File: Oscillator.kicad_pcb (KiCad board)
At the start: 2 copper layers, 19.3 x 14 mm, 11 parts, among them J1 Conn_01x01, J2 Conn_01x01, J3 Conn_01x01, J4 Conn_01x01, U1 74HC04, Y1 10 MHz

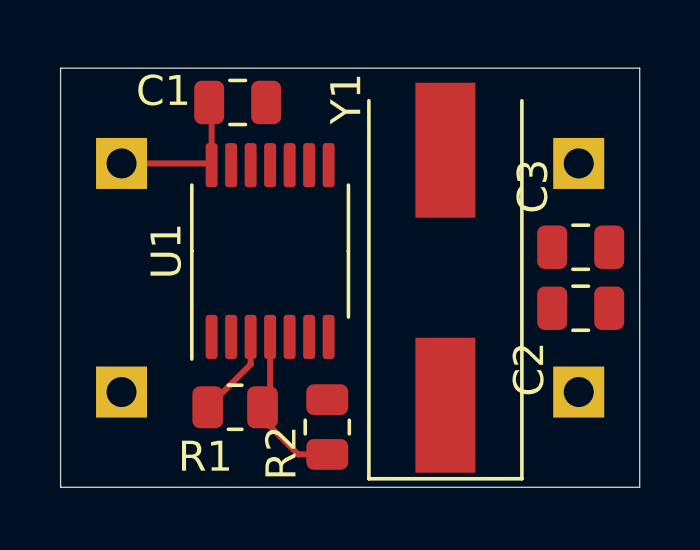
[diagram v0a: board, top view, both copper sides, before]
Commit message: routed all signals
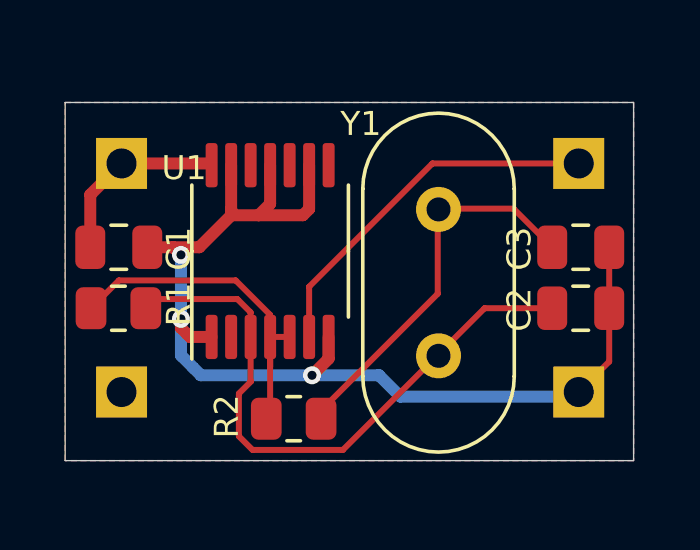
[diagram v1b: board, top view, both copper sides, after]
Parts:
- Y1: footprint Crystal:Crystal_SMD_HC49-SD -> Crystal:Crystal_HC49-U_Vertical
- moved C1 6.24 mm to (115.5, 95.5)
- moved R1 5.10 mm to (115.5, 97.5), turned to 180 degrees
- moved Y1 2.61 mm to (126.1, 99.1)
- moved R2 1.15 mm to (121.3, 101.2), turned to 0 degrees
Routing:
- net GND: track 0.00 -> 36.7 mm, vias 0 -> 3
- net Net-(C2-Pad1): track 2.94 -> 20.7 mm
- net Net-(C3-Pad1): track 0.00 -> 13.0 mm
- net /Out: track 0.00 -> 12.4 mm
- net Net-(R1-Pad2): track 5.48 -> 12.0 mm
- net VCC: track 5.15 -> 6.54 mm
- added copper zone on B.Cu, net GND
- added copper zone on F.Cu, net GND
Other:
- board size 19.3 x 14 mm -> 18.9 x 11.9 mm

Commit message: silkscreen improvements
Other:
- board text added: "github.com/daveho/ Oscillator"
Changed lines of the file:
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@@
     (property "ki_keywords" "HCMOS not inv")
     (attr smd)
-    (fp_text reference "U1" (at 2.7686 -2.8702 180) (layer "F.SilkS")
+    (fp_text reference "U1" (at 1.651 -3.429 180) (layer "F.SilkS")
         (effects (font (size 0.8 0.8) (thickness 0.15)))
     )
@@
     (property "ki_keywords" "quartz ceramic resonator oscillator")
     (attr through_hole)
-    (fp_text reference "Y1" (at 7.7332 -2.5908 180) (layer "F.SilkS")
+    (fp_text reference "Y1" (at 7.5808 -2.6924 180) (layer "F.SilkS")
         (effects (font (size 0.8 0.8) (thickness 0.15)))
     )
@@
     (property "ki_keywords" "connector")
     (attr through_hole)
-    (fp_text reference "J2" (at 2.667 0) (layer "B.SilkS")
-        (effects (font (size 1 1) (thickness 0.15)) (justify mirror))
+    (fp_text reference "J2" (at 2.032 -1.2192) (layer "F.SilkS")
+        (effects (font (size 0.8 0.8) (thickness 0.15)))
     )
     (fp_text value "Conn_01x01" (at 0 -2.33) (layer "B.Fab")
@@
     (property "ki_keywords" "connector")
     (attr through_hole)
-    (fp_text reference "J1" (at -0.381 2.032) (layer "B.SilkS")
-        (effects (font (size 1 1) (thickness 0.15)) (justify mirror))
+    (fp_text reference "J1" (at -1.9812 -1.27) (layer "F.SilkS")
+        (effects (font (size 0.8 0.8) (thickness 0.15)))
     )
     (fp_text value "Conn_01x01" (at 0 -2.33) (layer "B.Fab")
@@
     (property "ki_keywords" "connector")
     (attr through_hole)
-    (fp_text reference "J3" (at 3.048 0) (layer "B.SilkS")
-        (effects (font (size 1 1) (thickness 0.15)) (justify mirror))
+    (fp_text reference "J3" (at 1.7272 0.9652) (layer "F.SilkS")
+        (effects (font (size 0.8 0.8) (thickness 0.15)))
     )
     (fp_text value "Conn_01x01" (at 0 -2.33) (layer "B.Fab")
@@
     (property "ki_keywords" "connector")
     (attr through_hole)
-    (fp_text reference "J4" (at -1.016 -2.159) (layer "B.SilkS")
-        (effects (font (size 1 1) (thickness 0.15)) (justify mirror))
+    (fp_text reference "J4" (at -1.9812 1.016) (layer "F.SilkS")
+        (effects (font (size 0.8 0.8) (thickness 0.15)))
     )
     (fp_text value "Conn_01x01" (at 0 -2.33) (layer "B.Fab")
@@
   (gr_rect (start 113.6904 90.678) (end 132.6388 102.616)
     (stroke (width 0.0381) (type default)) (fill none) (layer "Edge.Cuts"))
+  (gr_text "github.com/daveho/\n  Oscillator" (at 131.0132 97.9424) (layer "B.SilkS")
+    (effects (font (size 1 1) (thickness 0.25) bold) (justify left bottom mirror))
+  )
   (segment (start 115.57 92.71) (end 114.5286 93.7514) (width 0.4) (layer "F.Cu") (net 1))
   (segment (start 118.5145 92.71) (end 118.573 92.7685) (width 0.2) (layer "F.Cu") (net 1))
